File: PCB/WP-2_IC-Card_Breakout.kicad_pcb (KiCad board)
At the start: 2 copper layers, 54 x 54 mm, 2 parts, among them J1 Conn_01x38_Female, J2 Conn_02x19_Odd_Even

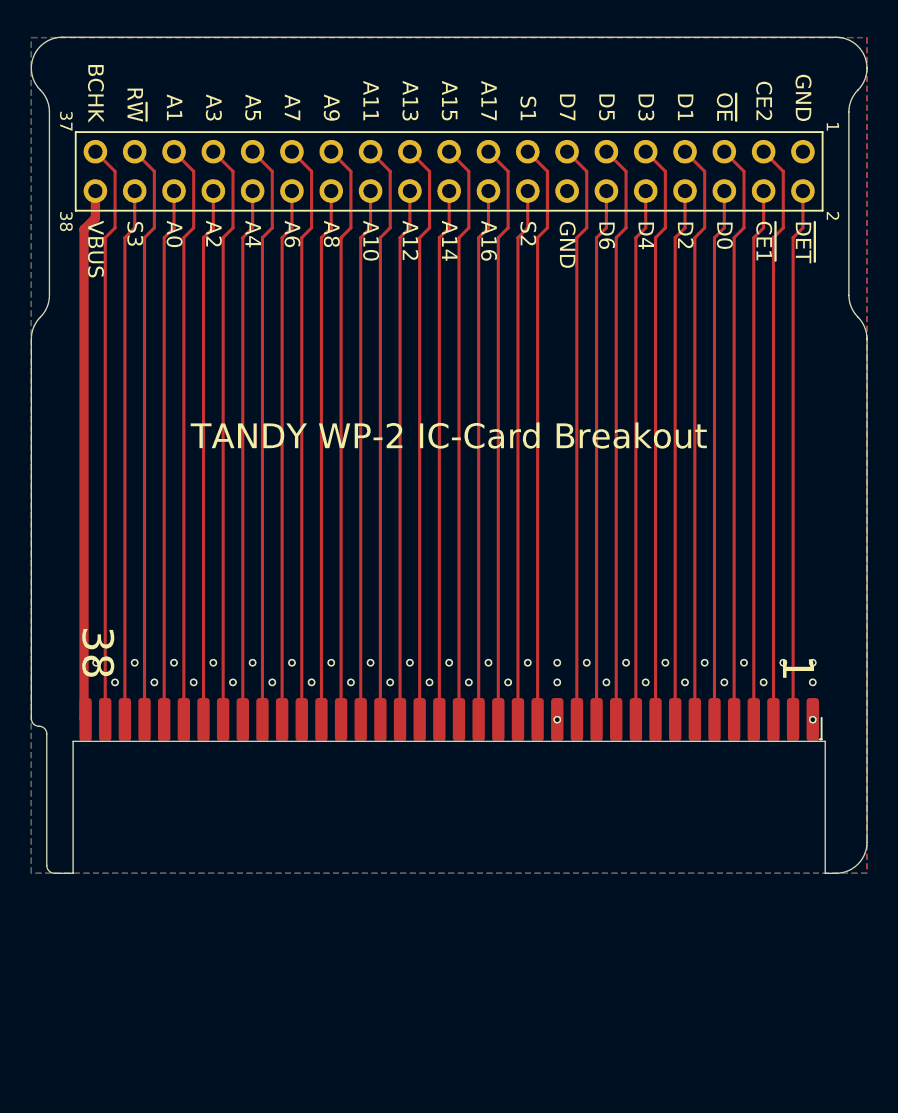
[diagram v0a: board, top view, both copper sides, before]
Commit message: simpler caps for ram card, 3d-printed cover, new WIP 4-bank MRAM card
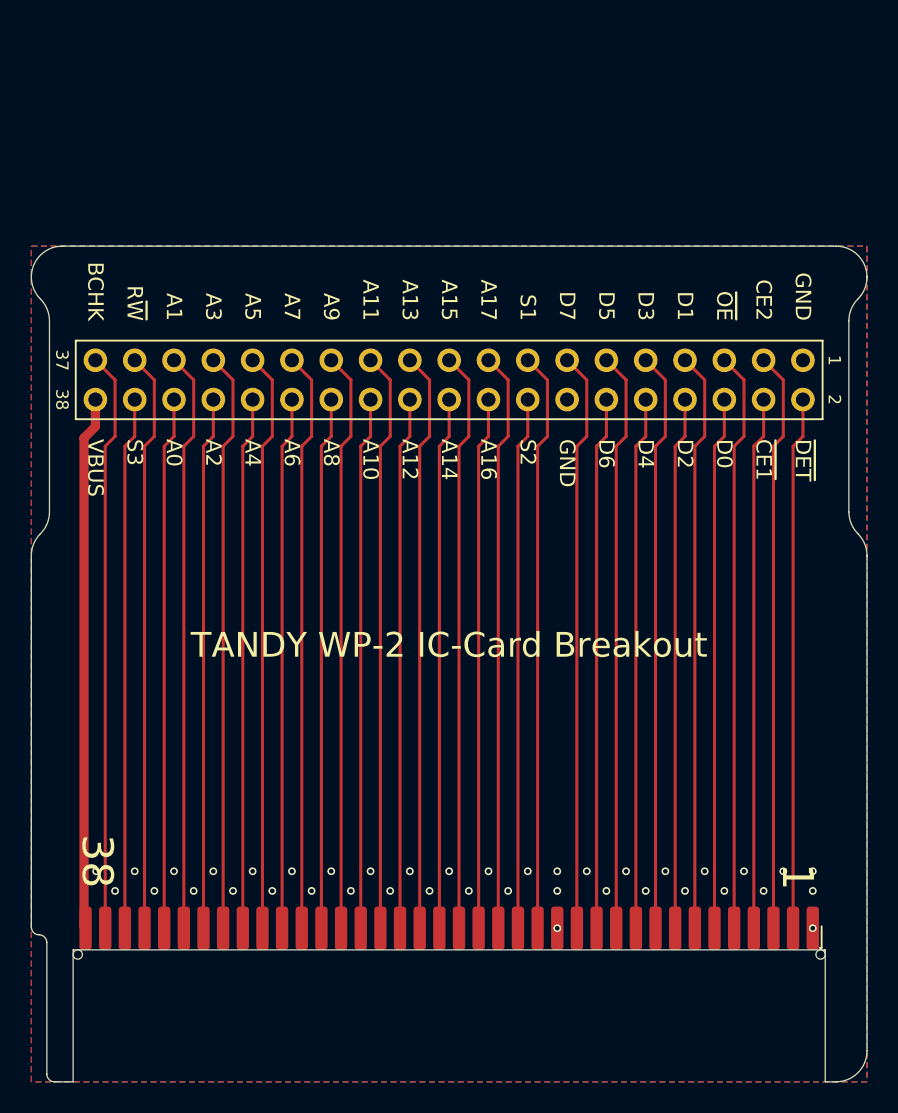
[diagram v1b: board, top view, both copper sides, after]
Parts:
- added REF**: npth_0.6mm, 0_LOCAL:npth_0.6mm, F.Cu at (163.7, 119.8)
- added REF**: npth_0.6mm, 0_LOCAL:npth_0.6mm, F.Cu at (115.7, 119.8)
- added REF**: WP-2_IC_Card_Cover_Breakout, 0_LOCAL:WP-2_IC_Card_Cover_Breakout, F.Cu at (139.7, 101.0)
- moved J2 13.5 mm to (162.6, 81.4)
- moved J1 13.5 mm to (139.7, 119.5)
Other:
- outline, holes or cut-outs redrawn

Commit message: MRAM level shifters, delete FRAM, local datasheets in local symbols
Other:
- board text added: "${COMMENT1}"
- board text added: "${TITLE}"
- board text added: "${TITLE} v${REVISION}"
- board text removed: "TANDY WP-2 IC-Card Breakout"
- board text removed: "WP-2_IC_Card_Breakout v004"
- board text removed: "github.com/bkw777/WP-2_IC_Card"

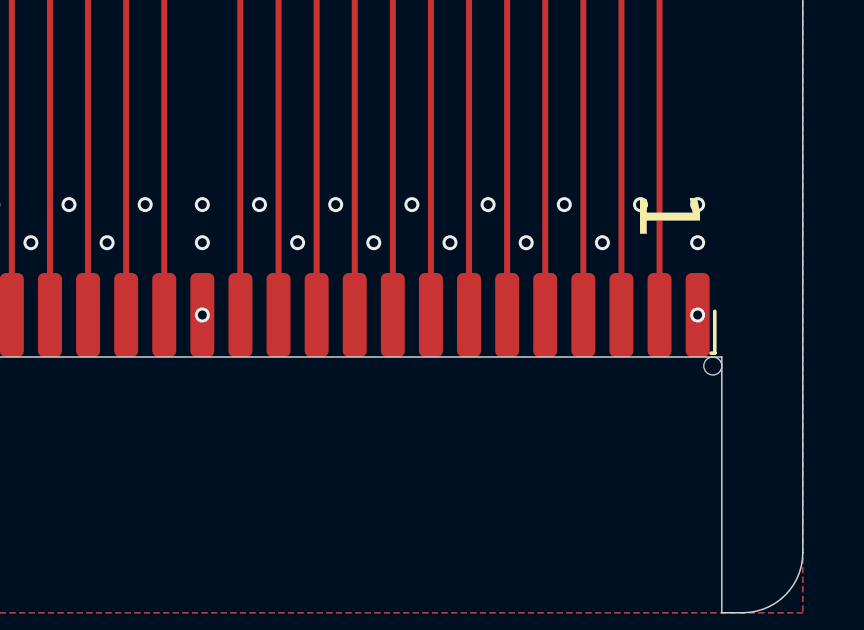
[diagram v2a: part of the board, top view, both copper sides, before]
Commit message: ram 128 move vias off pads and add MPN and fab_bom.csv
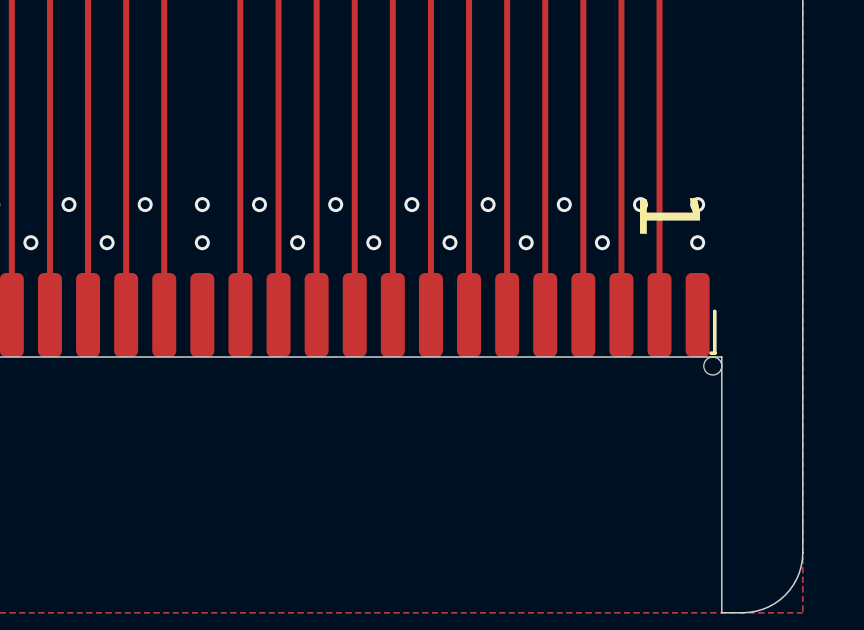
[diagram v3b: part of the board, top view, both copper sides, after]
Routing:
- net GND: vias 40 -> 38
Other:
- board text added: "Bottom Soldermask Full Coverage"
- board text added: "PCB THICKNESS 1.2mm"
- board text removed: "PCB thickness 1.2mm"

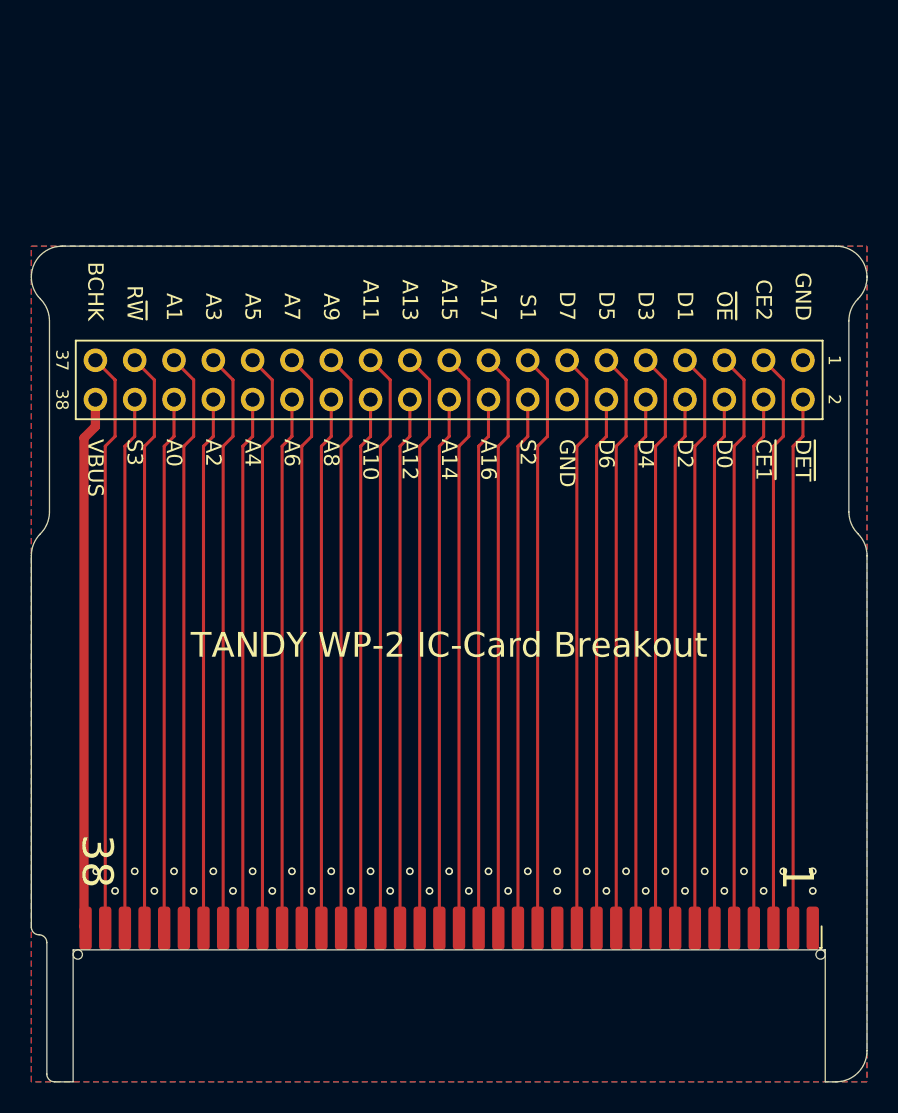
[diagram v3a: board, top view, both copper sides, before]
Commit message: local symbol & footprint library organization, add shielded mram version
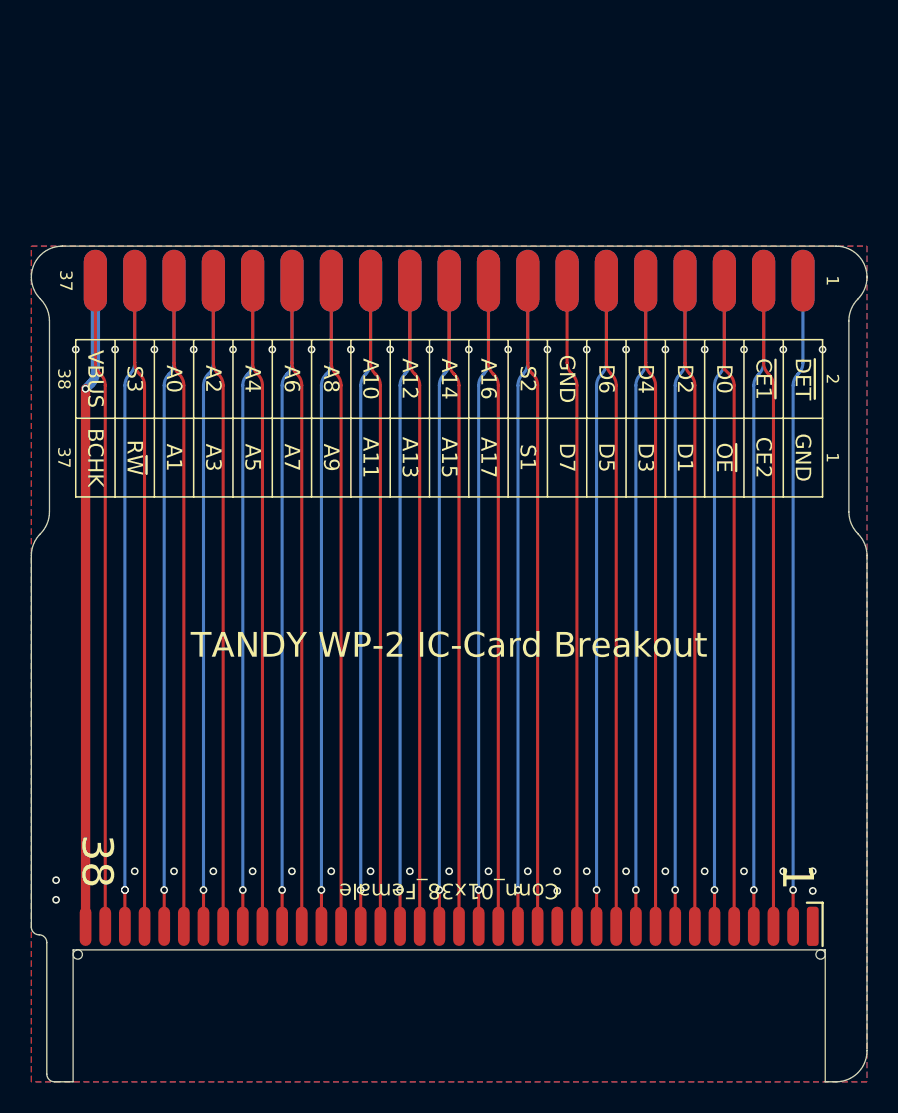
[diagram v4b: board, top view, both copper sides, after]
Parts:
- removed the REF** at (163.7, 119.8)
- removed the REF** at (115.7, 119.8)
- removed the REF** at (139.7, 101.0)
- added N1: WP-2_IC-Card_Cover_Breakout, 000_LOCAL:WP-2_IC_Card_Cover_Breakout, F.Cu at (139.7, 101.0)
- added REF**: npth_0.6mm, 000_LOCAL:npth_0.6mm, F.Cu at (163.7, 119.8)
- added REF**: npth_0.6mm, 000_LOCAL:npth_0.6mm, F.Cu at (115.7, 119.8)
- J1: footprint 0_LOCAL:SMS-138-01-x-x_edge -> 000_LOCAL:SMS-138-01-x-x_pcb_edge
- J2: value Conn_02x19_Odd_Even -> Conn_02x19_Odd_Even_PCB_Edge; footprint 0_LOCAL:PinHeader_2x19_P2.54mm -> 000_LOCAL:Pin-Header_2x19_P2.54mm_PCB_Edge
- moved J2 24.1 mm to (139.7, 73.9), turned to 90 degrees
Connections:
- J2 pad 1: GND -> /BCHK
- J2 pad 10: /D4 -> /A4
- J2 pad 11: /D5 -> /A7
- J2 pad 12: /D6 -> /A6
- J2 pad 13: /D7 -> /A9
- J2 pad 14: GND -> /A8
- J2 pad 15: /S1 -> /A11
- J2 pad 16: /S2 -> /A10
- J2 pad 17: /A17 -> /A13
- J2 pad 18: /A16 -> /A12
- J2 pad 2: /~{DET} -> VBUS
- J2 pad 21: /A13 -> /A17
- J2 pad 22: /A12 -> /A16
- J2 pad 23: /A11 -> /S1
- J2 pad 24: /A10 -> /S2
- J2 pad 25: /A9 -> /D7
- J2 pad 26: /A8 -> GND
- J2 pad 27: /A7 -> /D5
- J2 pad 28: /A6 -> /D6
- J2 pad 29: /A5 -> /D3
- J2 pad 3: /CE2 -> /R~{W}
- J2 pad 30: /A4 -> /D4
- J2 pad 31: /A3 -> /D1
- J2 pad 32: /A2 -> /D2
- J2 pad 33: /A1 -> /~{OE}
- J2 pad 34: /A0 -> /D0
- J2 pad 35: /R~{W} -> /CE2
- J2 pad 36: /S3 -> /~{CE1}
- J2 pad 37: /BCHK -> GND
- J2 pad 38: VBUS -> /~{DET}
- J2 pad 4: /~{CE1} -> /S3
- J2 pad 5: /~{OE} -> /A1
- J2 pad 6: /D0 -> /A0
- J2 pad 7: /D1 -> /A3
- J2 pad 8: /D2 -> /A2
- J2 pad 9: /D3 -> /A5
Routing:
- net /S2: track 34.4 -> 42.0 mm, vias 0 -> 1
- net /A10: track 34.4 -> 41.9 mm, vias 0 -> 1
- net /D0: track 34.4 -> 41.9 mm, vias 0 -> 1
- net /A4: track 34.4 -> 41.9 mm, vias 0 -> 1
- net /~{DET}: track 34.4 -> 41.9 mm, vias 0 -> 1
- net /S3: track 34.4 -> 41.9 mm, vias 0 -> 2
- net /A14: track 34.4 -> 41.9 mm, vias 0 -> 1
- net /D4: track 34.4 -> 41.9 mm, vias 0 -> 1
- net /D2: track 34.4 -> 41.9 mm, vias 0 -> 1
- net /A6: track 34.4 -> 41.9 mm, vias 0 -> 1
- net /~{CE1}: track 34.4 -> 41.9 mm, vias 0 -> 1
- net /D6: track 34.4 -> 41.9 mm, vias 0 -> 1
- net /A8: track 34.4 -> 41.9 mm, vias 0 -> 1
- net /A2: track 34.4 -> 41.9 mm, vias 0 -> 1
- net /A16: track 34.4 -> 41.9 mm, vias 0 -> 1
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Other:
- board text added: "BOARD OUTLINE"

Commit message: cleanup names, cover inside corner reliefs
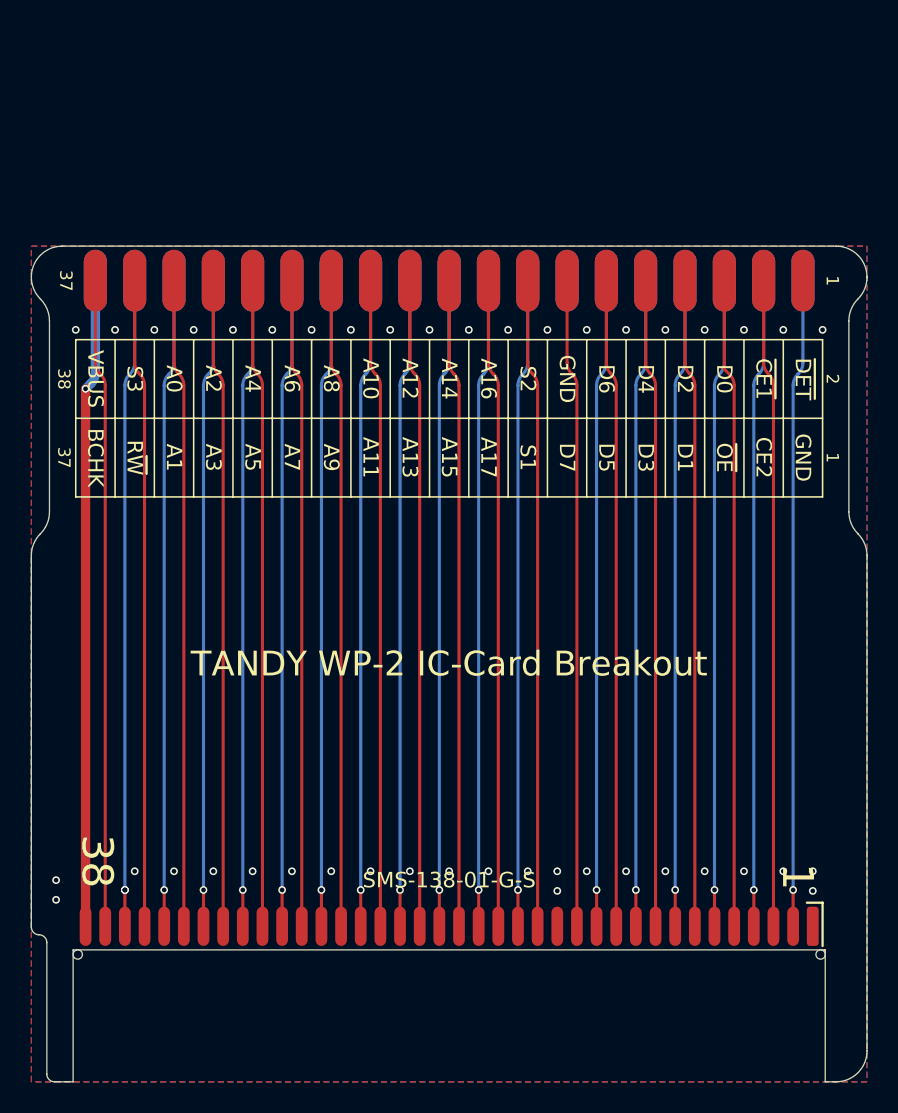
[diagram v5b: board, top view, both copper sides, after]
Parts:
- J1: value Conn_01x38_Female -> SMS-138-01-G-S
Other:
- board text removed: "Connector: Samtec SMS-138-01-G-S"

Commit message: rom name & revision
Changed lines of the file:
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@@
 	(paper "USLetter")
 	(title_block
-		(title "TANDY WP-2 IC-Card Breakout")
-		(date "2024-10-03")
+		(title "WP-2_IC-Card_Breakout")
+		(date "2024-10-04")
 		(rev "008")
 		(company "Brian K. White - b.kenyon.w@gmail.com")
@@
 		(fp_arc
 			(start 25.828427 -22.171574)
-			(mid 25.980661 -22.936945)
+			(mid 25.980667 -22.936939)
 			(end 26.414213 -23.585788)
 			(stroke
@@
 		(fp_arc
 			(start 26.414214 -8.414214)
-			(mid 25.98066 -9.063061)
+			(mid 25.98065 -9.063055)
 			(end 25.828427 -9.828428)
 			(stroke

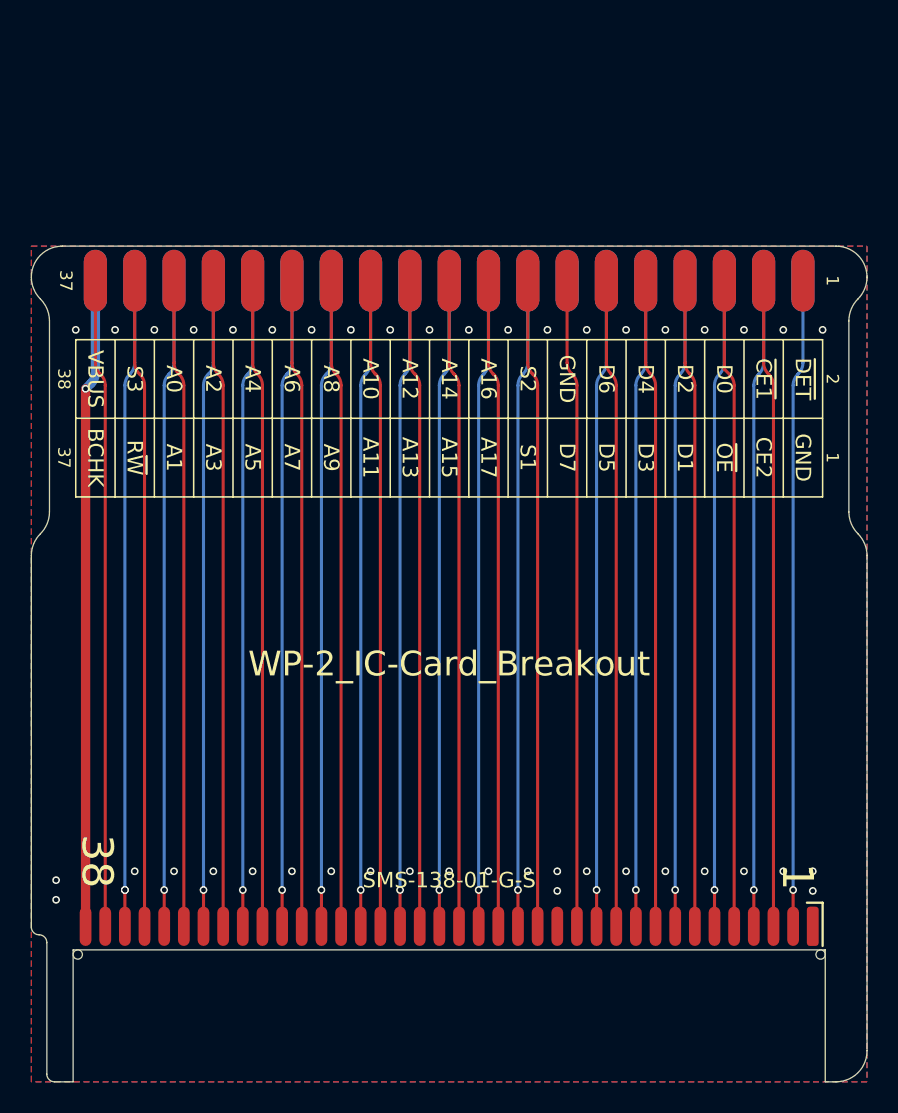
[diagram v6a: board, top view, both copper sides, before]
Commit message: redraw board outline and copy to all boards
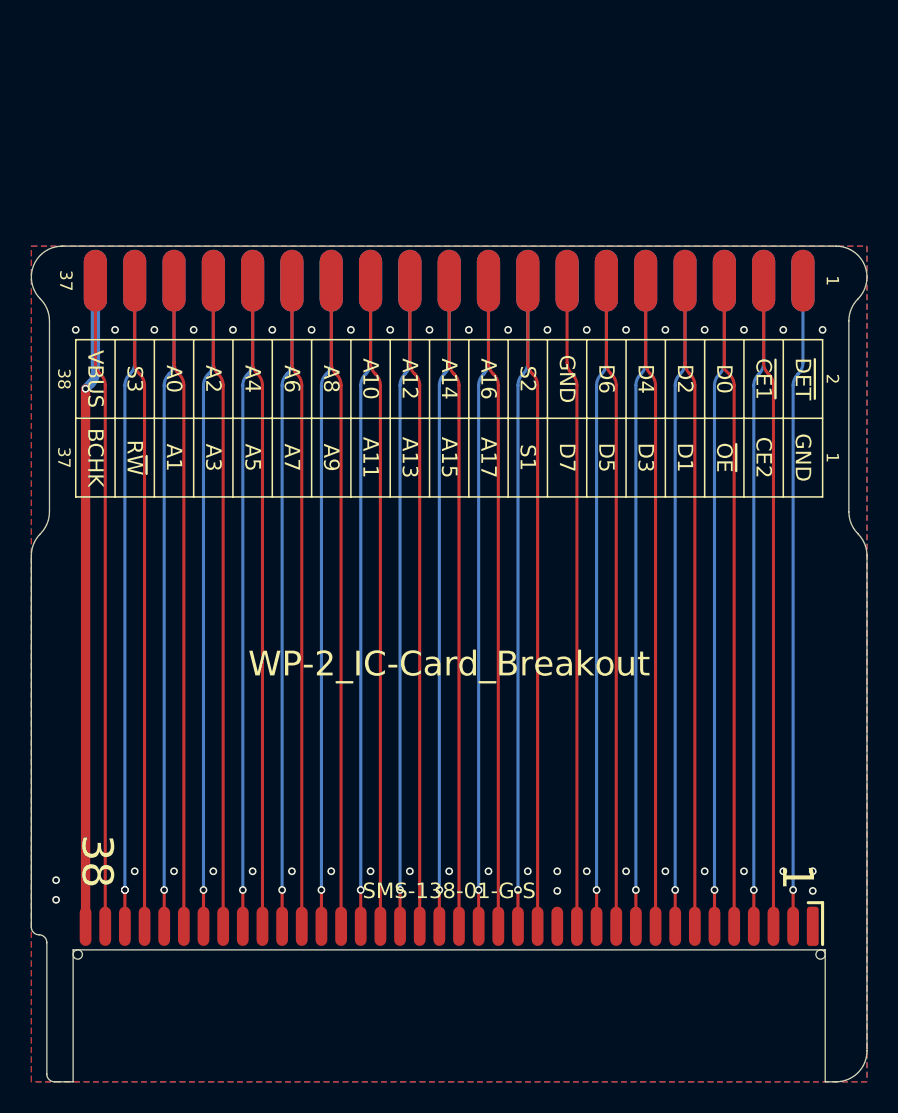
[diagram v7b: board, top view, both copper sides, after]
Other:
- outline, holes or cut-outs redrawn

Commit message: rom wren sw, boms, footprints, shielded mram
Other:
- board text added: "Max PCB Thickness: 1.2mm"
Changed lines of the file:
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@@
 		(fp_arc
 			(start 25.828427 -22.171574)
-			(mid 25.980661 -22.936945)
+			(mid 25.980667 -22.936939)
 			(end 26.414213 -23.585788)
 			(stroke
@@
 		(fp_arc
 			(start 26.414214 -8.414214)
-			(mid 25.980662 -9.063056)
+			(mid 25.98065 -9.063055)
 			(end 25.828427 -9.828428)
 			(stroke
@@
 			)
 		)
+	)
+	(gr_text "Max PCB Thickness: 1.2mm"
+		(at 169.7 101.045 270)
+		(layer "Eco1.User")
+		(effects
+			(font
+				(size 2 2)
+				(thickness 0.2)
+			)
+		)
